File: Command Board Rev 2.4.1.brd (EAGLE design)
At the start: 119.4 x 61 mm, 45 parts, among them IC1 PIC24FXXKA302_SPDIP, Q2-IRF510 IRF740

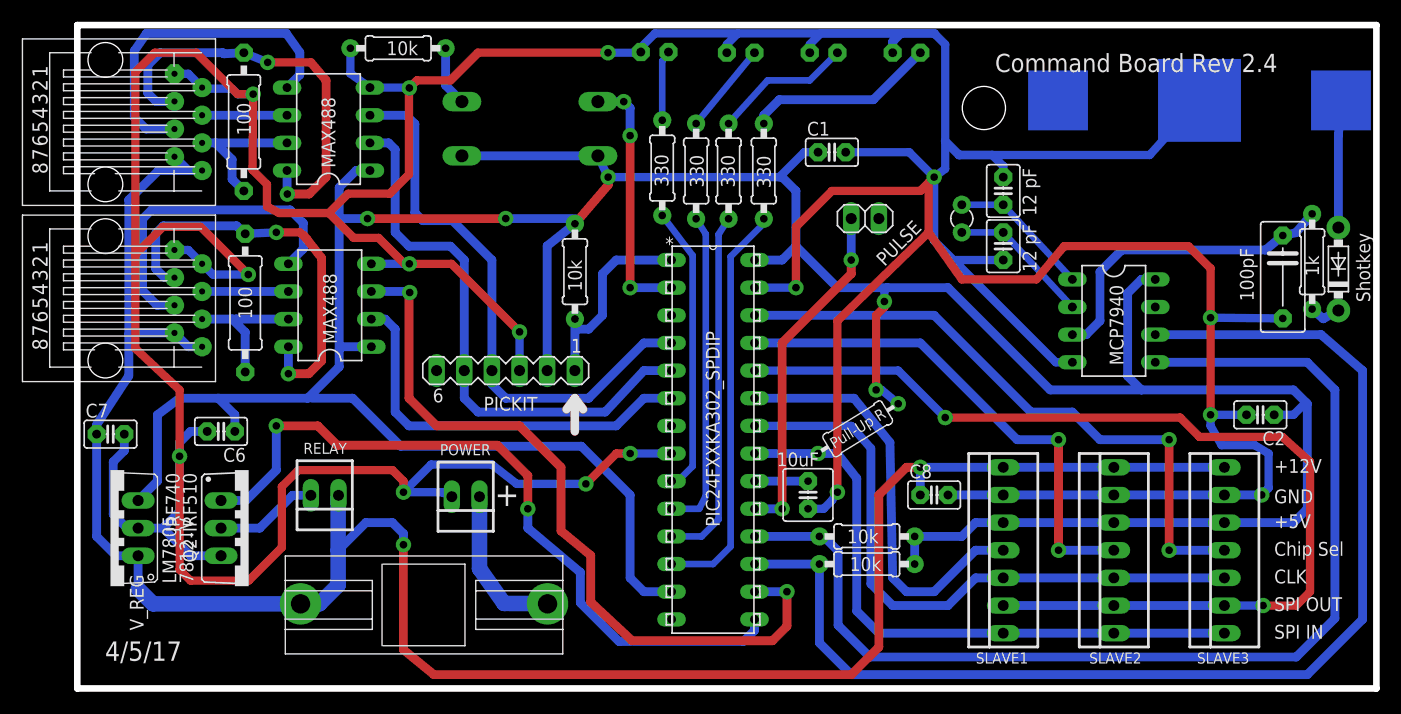
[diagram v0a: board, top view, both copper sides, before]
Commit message: Fix some design rules and vias
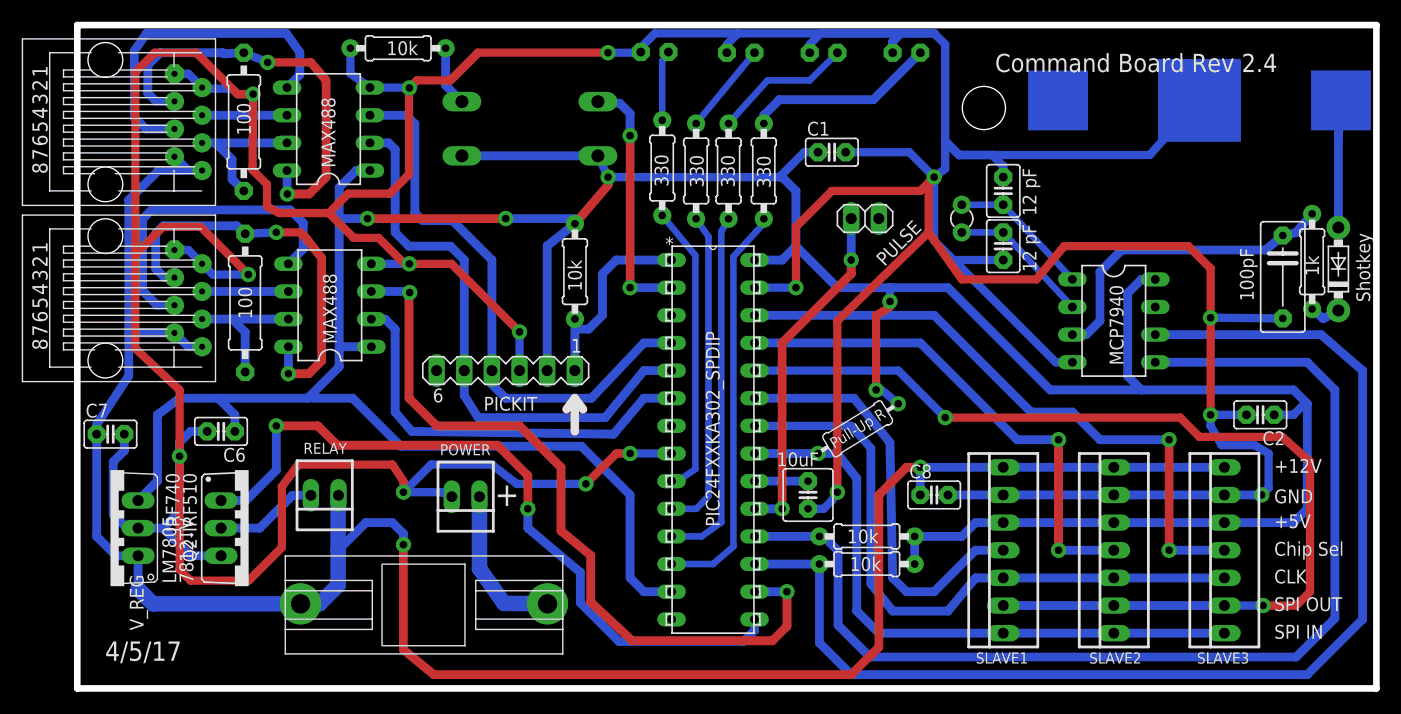
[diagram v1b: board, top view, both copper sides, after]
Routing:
- net GND: track 544.0 -> 544.8 mm
- net U1RX: track 37.2 -> 37.9 mm
- net SPI_SCK1: track 58.4 -> 59.2 mm
- net U2RX: track 51.5 -> 52.2 mm
- net EMER_BTN_IN: track 23.5 -> 23.2 mm, vias 3 -> 2
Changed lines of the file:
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@@
 <wire x1="97.79" y1="27.432" x2="89.408" y2="27.432" width="0.8128" layer="16"/>
 <wire x1="89.408" y1="27.432" x2="80.01" y2="36.83" width="0.8128" layer="16"/>
-<wire x1="80.01" y1="36.83" x2="74.422" y2="36.83" width="0.8128" layer="16"/>
-<wire x1="74.422" y1="36.83" x2="69.85" y2="36.83" width="0.8128" layer="16"/>
+<wire x1="80.01" y1="36.83" x2="74.676" y2="36.83" width="0.8128" layer="16"/>
+<wire x1="74.676" y1="36.83" x2="69.85" y2="36.83" width="0.8128" layer="16"/>
 <wire x1="69.85" y1="36.83" x2="66.04" y2="40.64" width="0.8128" layer="16"/>
 <wire x1="21.59" y1="26.67" x2="25.30475" y2="26.67" width="0.8128" layer="16"/>
@@
 <wire x1="7.366" y1="19.05" x2="5.588" y2="17.272" width="0.8128" layer="16"/>
 <via x="48.7807" y="46.99" extent="1-16" drill="0.7" diameter="1.4224" shape="square"/>
-<via x="74.168" y="35.56" extent="1-16" drill="0.7" diameter="1.4224" shape="square"/>
+<via x="74.676" y="35.56" extent="1-16" drill="0.7" diameter="1.4224" shape="square"/>
 <via x="73.406" y="27.432" extent="1-16" drill="0.7" diameter="1.4224" shape="square"/>
-<wire x1="74.168" y1="35.56" x2="74.168" y2="36.576" width="0.762" layer="16"/>
-<wire x1="74.168" y1="36.576" x2="74.422" y2="36.83" width="0.762" layer="16"/>
-<wire x1="74.168" y1="35.56" x2="74.168" y2="35.052" width="0.762" layer="1"/>
-<wire x1="74.168" y1="35.052" x2="73.406" y2="34.29" width="0.762" layer="1"/>
+<wire x1="74.676" y1="35.56" x2="74.676" y2="36.83" width="0.762" layer="16"/>
+<wire x1="74.676" y1="35.56" x2="74.676" y2="35.052" width="0.762" layer="1"/>
+<wire x1="74.676" y1="35.052" x2="73.406" y2="34.29" width="0.762" layer="1"/>
 <wire x1="73.406" y1="34.29" x2="73.406" y2="27.432" width="0.762" layer="1"/>
 <via x="75.438" y="26.162" extent="1-16" drill="0.7" diameter="1.4224" shape="square"/>
@@
 <signal name="EMER_BTN_IN">
 <contactref element="IC1" pad="2"/>
-<wire x1="50.2158" y1="53.9242" x2="50.8" y2="53.34" width="0.8128" layer="16"/>
-<wire x1="50.8" y1="53.34" x2="50.8" y2="50.8" width="0.8128" layer="16"/>
+<wire x1="49.8602" y1="53.7718" x2="50.8" y2="52.832" width="0.8128" layer="16"/>
+<wire x1="50.8" y1="52.832" x2="50.8" y2="50.8" width="0.8128" layer="16"/>
 <via x="50.8" y="50.8" extent="1-16" drill="0.7" diameter="1.4224" shape="square"/>
 <wire x1="50.8" y1="50.8" x2="50.8" y2="36.83" width="0.8128" layer="1"/>
 <via x="50.8" y="36.83" extent="1-16" drill="0.7" diameter="1.4224" shape="square"/>
 <wire x1="50.8" y1="36.83" x2="54.61" y2="36.83" width="0.8128" layer="16"/>
-<via x="50.2158" y="53.9242" extent="1-16" drill="0.7" diameter="1.4224" shape="square"/>
 <contactref element="S1" pad="1"/>
-<wire x1="47.8409" y1="53.9242" x2="50.2158" y2="53.9242" width="0.8128" layer="16"/>
+<wire x1="47.8409" y1="53.9242" x2="49.8602" y2="53.7718" width="0.8128" layer="16"/>
 </signal>
 <signal name="GND">
@@
 <wire x1="27.01925" y1="39.02075" x2="30.51175" y2="39.02075" width="0.762" layer="16"/>
 <wire x1="29.972" y1="18.034" x2="29.972" y2="19.05" width="0.762" layer="1"/>
-<wire x1="29.972" y1="19.05" x2="28.956" y2="20.066" width="0.762" layer="1"/>
-<wire x1="28.956" y1="20.066" x2="20.32" y2="20.066" width="0.762" layer="1"/>
-<wire x1="20.32" y1="20.066" x2="18.796" y2="18.542" width="0.762" layer="1"/>
+<wire x1="29.972" y1="19.05" x2="28.956" y2="20.574" width="0.762" layer="1"/>
+<wire x1="28.956" y1="20.574" x2="20.32" y2="20.574" width="0.762" layer="1"/>
+<wire x1="20.32" y1="20.574" x2="18.796" y2="18.542" width="0.762" layer="1"/>
 <wire x1="18.796" y1="18.542" x2="18.796" y2="12.954" width="0.762" layer="1"/>
 <wire x1="18.796" y1="12.954" x2="15.748" y2="9.906" width="0.762" layer="1"/>
@@
 <wire x1="34.29" y1="40.64" x2="35.56" y2="39.37" width="0.8128" layer="16"/>
 <wire x1="35.56" y1="39.37" x2="35.56" y2="29.21" width="0.8128" layer="16"/>
-<wire x1="35.56" y1="29.21" x2="35.56" y2="26.67" width="0.8128" layer="16"/>
-<wire x1="35.56" y1="26.67" x2="36.83" y2="25.4" width="0.8128" layer="16"/>
-<wire x1="36.83" y1="25.4" x2="48.514" y2="25.4" width="0.8128" layer="16"/>
-<wire x1="48.514" y1="25.4" x2="52.07" y2="29.21" width="0.8128" layer="16"/>
+<wire x1="35.56" y1="29.21" x2="35.56" y2="26.924" width="0.8128" layer="16"/>
+<wire x1="35.56" y1="26.924" x2="36.83" y2="24.892" width="0.8128" layer="16"/>
+<wire x1="36.83" y1="24.892" x2="48.514" y2="24.892" width="0.8128" layer="16"/>
+<wire x1="48.514" y1="24.892" x2="52.07" y2="29.21" width="0.8128" layer="16"/>
 <wire x1="52.07" y1="29.21" x2="54.61" y2="29.21" width="0.8128" layer="16"/>
 </signal>
@@
 <wire x1="38.1" y1="29.21" x2="38.1" y2="27.94" width="0.8128" layer="16"/>
 <wire x1="38.1" y1="27.94" x2="39.37" y2="26.67" width="0.8128" layer="16"/>
-<wire x1="39.37" y1="26.67" x2="46.99" y2="26.67" width="0.8128" layer="16"/>
-<wire x1="46.99" y1="26.67" x2="52.07" y2="31.75" width="0.8128" layer="16"/>
+<wire x1="39.37" y1="26.67" x2="47.244" y2="26.67" width="0.8128" layer="16"/>
+<wire x1="47.244" y1="26.67" x2="52.07" y2="31.75" width="0.8128" layer="16"/>
 <wire x1="52.07" y1="31.75" x2="54.61" y2="31.75" width="0.8128" layer="16"/>
 </signal>
@@
 <wire x1="28.28925" y1="33.94075" x2="29.21" y2="33.02" width="0.8128" layer="16"/>
 <wire x1="29.21" y1="33.02" x2="29.21" y2="25.4" width="0.8128" layer="16"/>
-<wire x1="29.21" y1="25.4" x2="30.48" y2="24.13" width="0.8128" layer="16"/>
-<wire x1="30.48" y1="24.13" x2="49.53" y2="24.13" width="0.8128" layer="16"/>
-<wire x1="49.53" y1="24.13" x2="52.07" y2="26.67" width="0.8128" layer="16"/>
+<wire x1="29.21" y1="25.4" x2="30.734" y2="23.622" width="0.8128" layer="16"/>
+<wire x1="30.734" y1="23.622" x2="49.276" y2="23.368" width="0.8128" layer="16"/>
+<wire x1="49.276" y1="23.368" x2="52.07" y2="26.67" width="0.8128" layer="16"/>
 <wire x1="52.07" y1="26.67" x2="54.61" y2="26.67" width="0.8128" layer="16"/>
 </signal>
@@
 <wire x1="95.25" y1="10.16" x2="105.41" y2="10.16" width="0.8128" layer="16"/>
 <wire x1="72.92975" y1="9.62025" x2="72.92975" y2="22.06625" width="0.8128" layer="16"/>
-<wire x1="72.92975" y1="9.62025" x2="74.93" y2="7.62" width="0.8128" layer="16"/>
-<wire x1="74.93" y1="7.62" x2="80.01" y2="7.62" width="0.8128" layer="16"/>
-<wire x1="80.01" y1="7.62" x2="82.55" y2="10.16" width="0.8128" layer="16"/>
+<wire x1="72.92975" y1="9.62025" x2="74.93" y2="7.112" width="0.8128" layer="16"/>
+<wire x1="74.93" y1="7.112" x2="80.01" y2="7.112" width="0.8128" layer="16"/>
+<wire x1="80.01" y1="7.112" x2="82.55" y2="10.16" width="0.8128" layer="16"/>
 <wire x1="82.55" y1="10.16" x2="85.09" y2="10.16" width="0.8128" layer="16"/>
 <wire x1="62.23" y1="24.13" x2="71.12" y2="24.13" width="0.762" layer="16"/>
@@
 <contactref element="IC1" pad="12"/>
 <wire x1="63.08725" y1="43.16095" x2="62.992" y2="42.64025" width="0.6096" layer="16"/>
-<wire x1="62.992" y1="42.64025" x2="60.03925" y2="39.6875" width="0.6096" layer="16"/>
-<wire x1="60.03925" y1="39.6875" x2="60.03925" y2="13.04925" width="0.6096" layer="16"/>
-<wire x1="60.03925" y1="13.04925" x2="58.42" y2="11.43" width="0.6096" layer="16"/>
+<wire x1="62.992" y1="42.64025" x2="60.29325" y2="39.6875" width="0.6096" layer="16"/>
+<wire x1="60.29325" y1="39.6875" x2="60.29325" y2="13.04925" width="0.6096" layer="16"/>
+<wire x1="60.29325" y1="13.04925" x2="58.42" y2="11.43" width="0.6096" layer="16"/>
 <wire x1="58.42" y1="11.43" x2="54.61" y2="11.43" width="0.6096" layer="16"/>
 </signal>
@@
 <contactref element="IC1" pad="11"/>
 <wire x1="54.61" y1="13.97" x2="57.37225" y2="13.97" width="0.6096" layer="16"/>
-<wire x1="57.37225" y1="13.97" x2="58.928" y2="15.52575" width="0.6096" layer="16"/>
-<wire x1="58.928" y1="15.52575" x2="58.928" y2="41.7195" width="0.6096" layer="16"/>
-<wire x1="58.928" y1="41.7195" x2="59.84875" y2="43.16095" width="0.6096" layer="16"/>
+<wire x1="57.37225" y1="13.97" x2="59.182" y2="15.27175" width="0.6096" layer="16"/>
+<wire x1="59.182" y1="15.27175" x2="59.182" y2="41.9735" width="0.6096" layer="16"/>
+<wire x1="59.182" y1="41.9735" x2="59.84875" y2="43.16095" width="0.6096" layer="16"/>
 </signal>
 <signal name="LED1">
@@
 <contactref element="IC1" pad="9"/>
 <wire x1="54.61" y1="19.05" x2="55.1815" y2="19.05" width="0.6096" layer="16"/>
-<wire x1="55.1815" y1="19.05" x2="56.54675" y2="20.41525" width="0.6096" layer="16"/>
-<wire x1="56.54675" y1="20.41525" x2="56.54675" y2="39.78275" width="0.6096" layer="16"/>
-<wire x1="56.54675" y1="39.78275" x2="53.75275" y2="43.46575" width="0.6096" layer="16"/>
+<wire x1="55.1815" y1="19.05" x2="56.80075" y2="20.16125" width="0.6096" layer="16"/>
+<wire x1="56.80075" y1="20.16125" x2="56.80075" y2="39.78275" width="0.6096" layer="16"/>
+<wire x1="56.80075" y1="39.78275" x2="53.75275" y2="43.46575" width="0.6096" layer="16"/>
 </signal>
 <signal name="LED2">
 <contactref element="R3" pad="1"/>
 <contactref element="IC1" pad="10"/>
-<wire x1="54.61" y1="16.51" x2="57.15" y2="16.51" width="0.6096" layer="16"/>
-<wire x1="57.15" y1="16.51" x2="57.75325" y2="17.68475" width="0.6096" layer="16"/>
-<wire x1="57.75325" y1="17.68475" x2="57.75325" y2="41.75125" width="0.6096" layer="16"/>
-<wire x1="57.75325" y1="41.75125" x2="56.86425" y2="43.16095" width="0.6096" layer="16"/>
+<wire x1="54.61" y1="16.51" x2="56.896" y2="16.51" width="0.6096" layer="16"/>
+<wire x1="56.896" y1="16.51" x2="58.00725" y2="17.68475" width="0.6096" layer="16"/>
+<wire x1="58.00725" y1="17.68475" x2="58.00725" y2="41.49725" width="0.6096" layer="16"/>
+<wire x1="58.00725" y1="41.49725" x2="56.86425" y2="43.16095" width="0.6096" layer="16"/>
 </signal>
 <signal name="N$8">

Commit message: Command Board PCB revised
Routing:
- net VCC: track 317.4 -> 322.7 mm
